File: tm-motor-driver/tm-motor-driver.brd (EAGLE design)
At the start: 50 x 30.1 mm, 18 parts

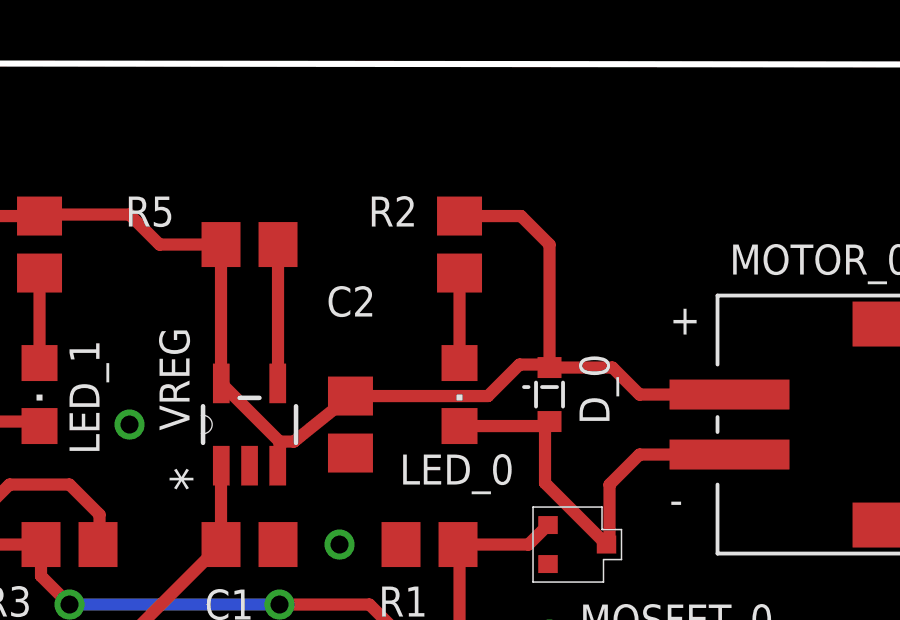
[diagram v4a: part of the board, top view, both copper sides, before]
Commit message: Fix LED_0 clearance error
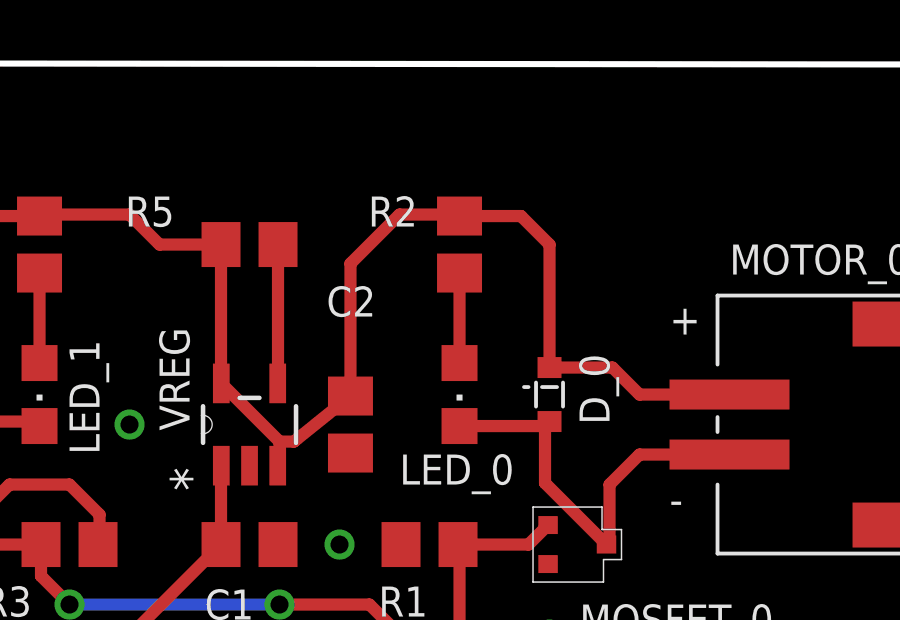
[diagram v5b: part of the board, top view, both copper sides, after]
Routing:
- net +3V3: track 52.9 -> 54.5 mm
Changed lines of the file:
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@@
 <wire x1="26" y1="17.4318" x2="26.4818" y2="17.4318" width="0.4064" layer="1"/>
 <wire x1="26.4818" y1="17.4318" x2="28.365" y2="18.95" width="0.4064" layer="1"/>
-<wire x1="28.365" y1="18.95" x2="32.95" y2="18.95" width="0.4064" layer="1"/>
-<wire x1="32.95" y1="18.95" x2="34" y2="20" width="0.4064" layer="1"/>
-<wire x1="34" y1="20" x2="34.9" y2="20" width="0.4064" layer="1"/>
-<wire x1="34.9" y1="20" x2="35" y2="19.9" width="0.4064" layer="1"/>
+<wire x1="28.365" y1="18.95" x2="28.365" y2="23.365" width="0.4064" layer="1"/>
+<wire x1="28.365" y1="23.365" x2="30" y2="25" width="0.4064" layer="1"/>
+<wire x1="30" y1="25" x2="31.95" y2="25" width="0.4064" layer="1"/>
+<wire x1="31.95" y1="25" x2="32" y2="24.95" width="0.4064" layer="1"/>
 </signal>
 <signal name="N$2">

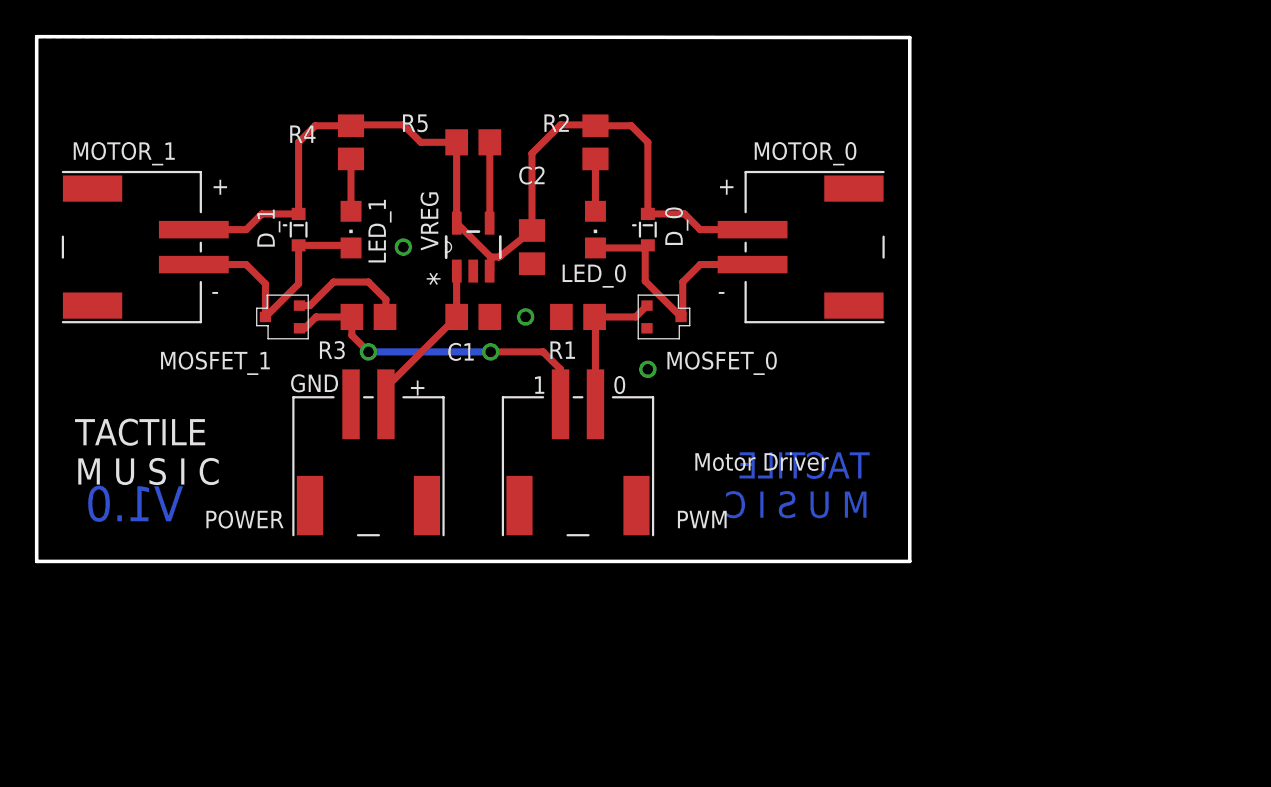
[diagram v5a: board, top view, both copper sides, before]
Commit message: Reduce board size
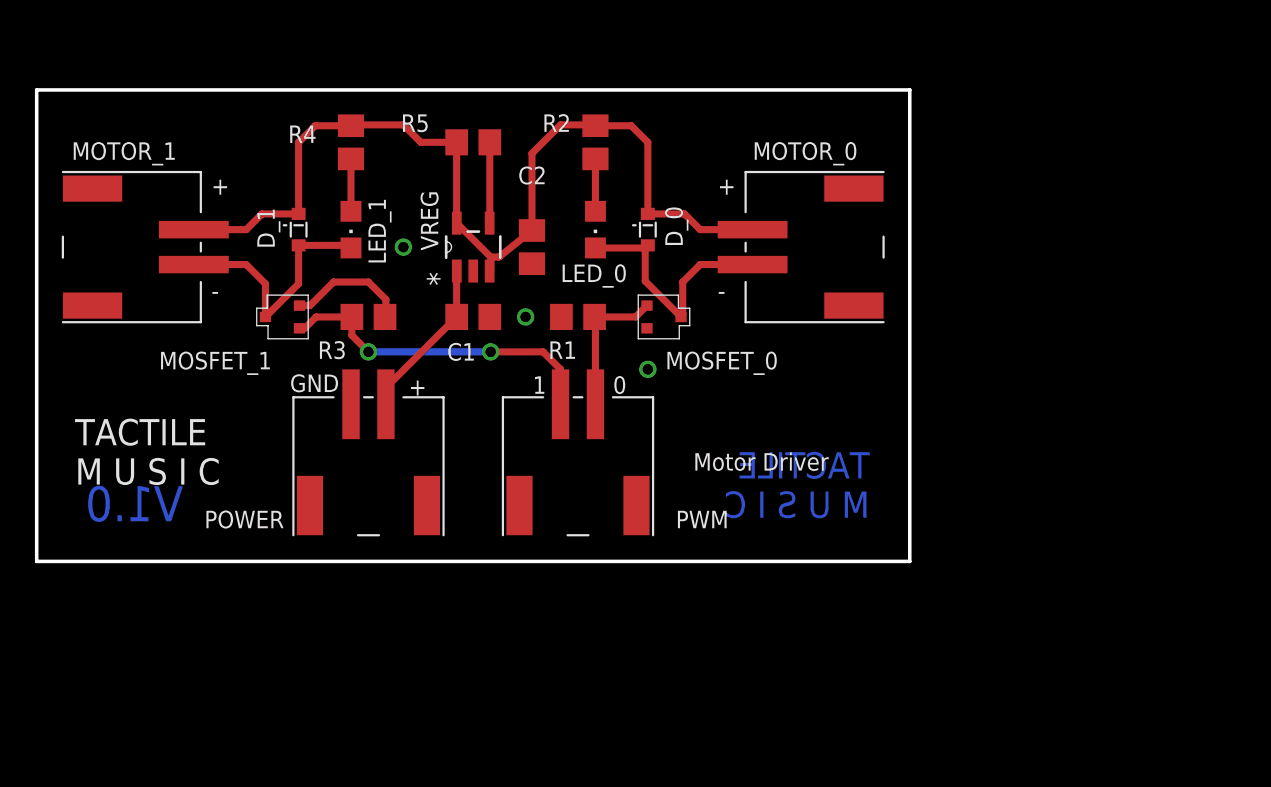
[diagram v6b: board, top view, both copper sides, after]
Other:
- board size 50 x 30.1 mm -> 50 x 27 mm
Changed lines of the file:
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@@
 <board>
 <plain>
-<wire x1="0" y1="0" x2="0" y2="30.05" width="0.2032" layer="20"/>
-<wire x1="0" y1="30.05" x2="50" y2="30" width="0.2032" layer="20"/>
-<wire x1="50" y1="30" x2="50" y2="0" width="0.2032" layer="20"/>
+<wire x1="0" y1="0" x2="0" y2="27" width="0.2032" layer="20"/>
+<wire x1="0" y1="27" x2="50" y2="27" width="0.2032" layer="20"/>
+<wire x1="50" y1="27" x2="50" y2="0" width="0.2032" layer="20"/>
 <wire x1="50" y1="0" x2="0" y2="0" width="0.2032" layer="20"/>
 <text x="21.3" y="9.5" size="1" layer="21" font="vector" ratio="20">+</text>
@@
 <polygon width="0.4064" layer="1" isolate="0.3048">
 <vertex x="0" y="0"/>
-<vertex x="0" y="30"/>
-<vertex x="50" y="30"/>
+<vertex x="0" y="27"/>
+<vertex x="50" y="27"/>
 <vertex x="50" y="0"/>
 </polygon>
 <polygon width="0.4064" layer="16" isolate="0.3048">
 <vertex x="0" y="0"/>
-<vertex x="0" y="30"/>
-<vertex x="50" y="30"/>
+<vertex x="0" y="27"/>
+<vertex x="50" y="27"/>
 <vertex x="50" y="0"/>
 </polygon>
